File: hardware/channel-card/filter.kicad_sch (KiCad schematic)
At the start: 117 parts, among them J181 CUTOFF CV 1 V/oct, SW181 FILTER BYPASS (latching), U101 SSI2144, U102 SSI2144, U103 LM13700, U104 NE5532, U105 NE5532, U106 NE5532, U107 TL072, U108 DG413DY

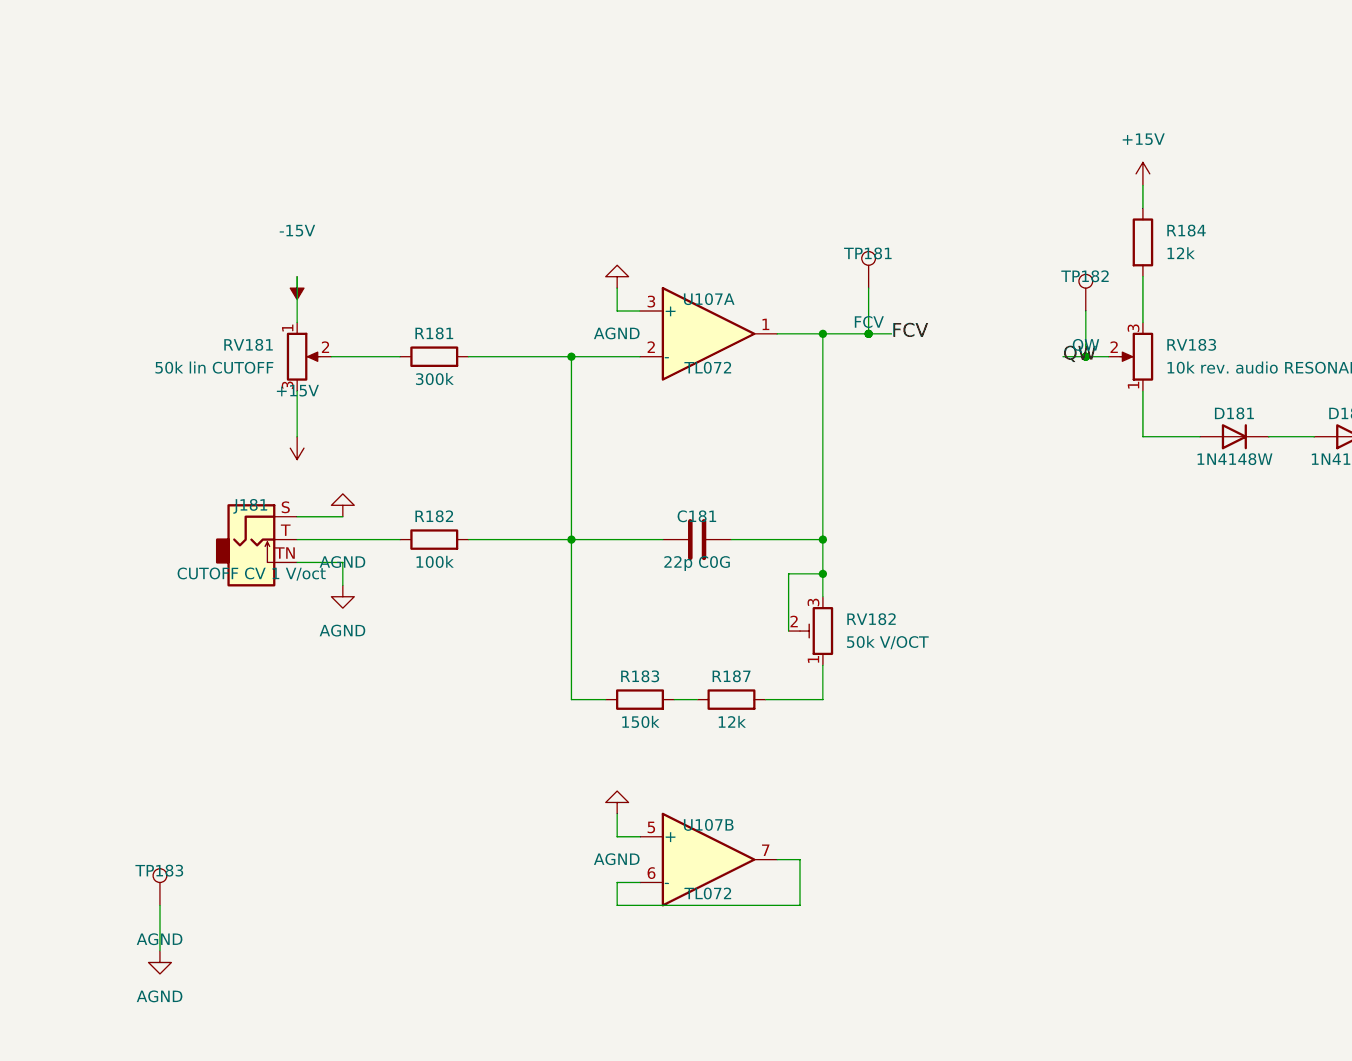
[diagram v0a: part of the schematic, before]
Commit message: Channel: cutoff CV chaining, CV OUT and summer clamp (decision 165)
CV OUT jack J182 reports the channel's total cutoff control at 1 V/oct
from FCV through the spare U107B. Jumper JP181 selects CV ONLY (a
plugged CV replaces the knob through J181's normal contact) or CV + POT.
D184/D185 BZT52C11 back to back clamp the cutoff summer so the SSI2144
frequency pin stays within about +-128 mV (datasheet range -120..+150 mV,
dropout above about +175 mV); simulation/cutoff/, breadboard test 13.
Panel row for CV IN/OUT noted for /system.

Co-Authored-By: Claude Opus 5.5 <noreply@anthropic.com>
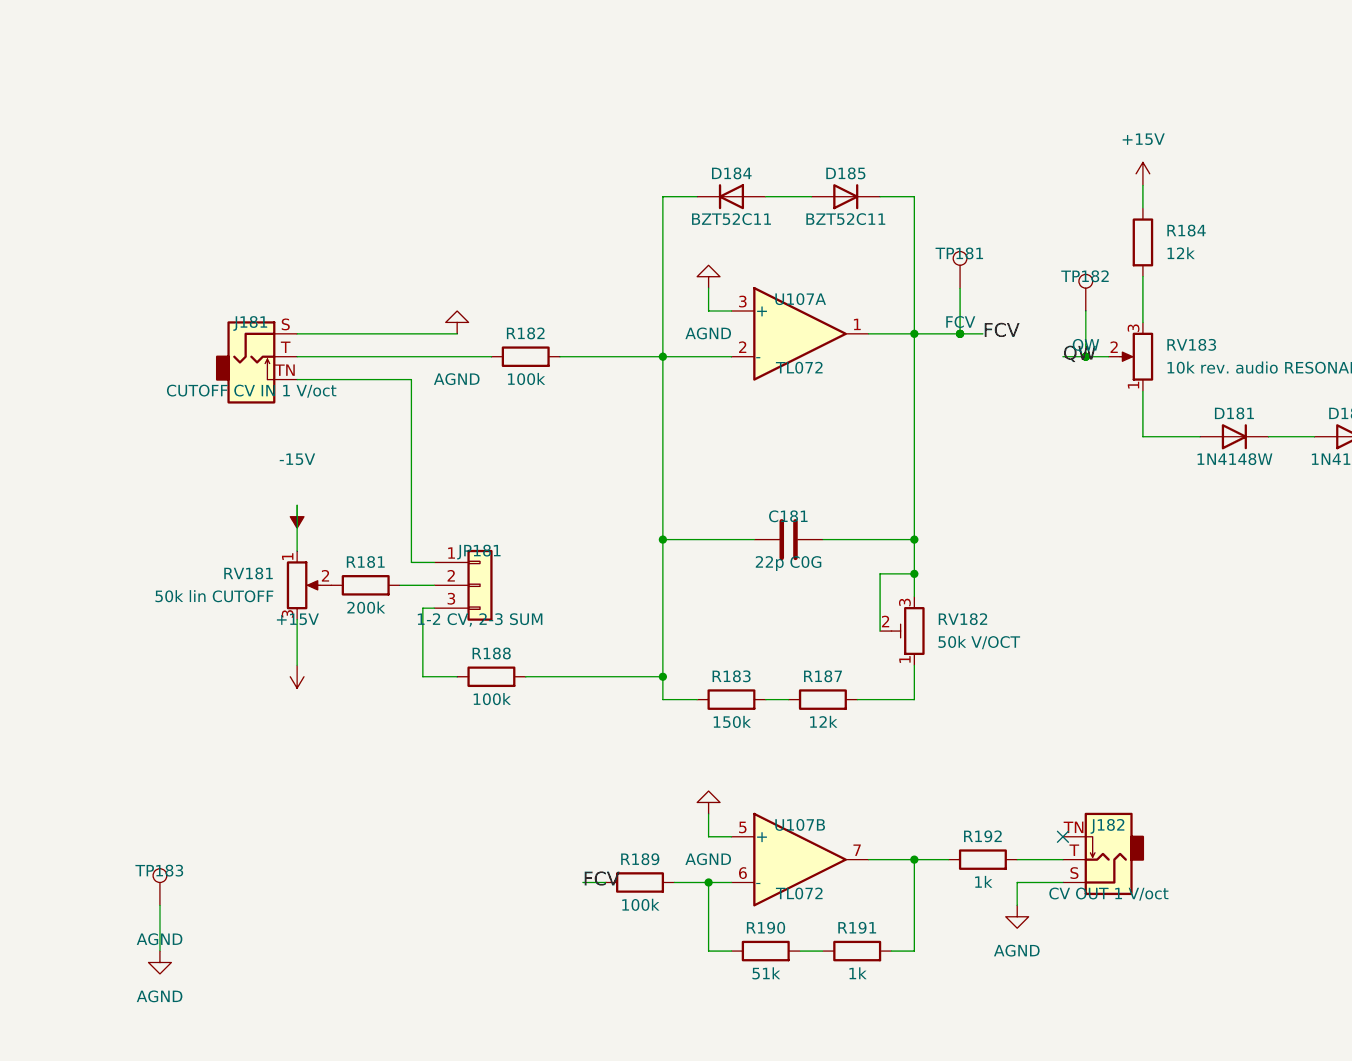
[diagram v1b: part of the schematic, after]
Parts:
- added D184, D185: BZT52C11, Diode_SMD:D_SOD-123, symbol Device:D
- added J182: CV OUT 1 V/oct, Connector_Audio:Jack_3.5mm_QingPu_WQP-PJ398SM_Vertical_CircularHoles, symbol Connector_Audio:AudioJack2_SwitchT
- added JP181: 1-2 CV, 2-3 SUM, Connector_PinHeader_2.54mm:PinHeader_1x03_P2.54mm_Vertical, symbol Connector_Generic:Conn_01x03
- added R188, R189: 100k, Resistor_SMD:R_0805_2012Metric, symbol Device:R
- added R190: 51k, Resistor_SMD:R_0805_2012Metric, symbol Device:R
- added R191, R192: 1k, Resistor_SMD:R_0805_2012Metric, symbol Device:R
- J181: value CUTOFF CV 1 V/oct -> CUTOFF CV IN 1 V/oct; Note 3.5 mm Thonkiconn on the top panel with a 1 mm M6 washer (SX-MECH-004); 3 mm PCB hole under the barrel -> 3.5 mm Thonkiconn on the top panel with a 1 mm M6 washer (SX-MECH-004); 3 mm PCB hole under the barrel; normal contact TN to JP181 (decision 165)
- R181: value 300k -> 200k; Note (none) -> With R188 100k the pot leg is 300k in either jumper positio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; ProjectPN SX-R-096 -> SX-R-116
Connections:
- net AGND: now also J182.S; no longer J181.TN
- net FCV: now also D185.1 (K), R189.1
- net at C181.1, R182.2, R183.1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: now also D184.1 (K), R188.2; no longer R181.2
- net at U107.7: now also R191.2, R192.1; no longer U107.6 (-)
- new net: J182.T, R192.2
- new net: JP181.2 (Pin_2), R181.2
- new net: D184.2 (A), D185.2 (A)
- new net: JP181.3 (Pin_3), R188.1
- new net: R190.2, R191.1
- new net: J181.TN, JP181.1 (Pin_1)
- new net: R189.2, R190.1, U107.6 (-)
- no-connect marks 6 -> 7

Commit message: Channel card: CD4052B bus assign, PFL and SC send switches at the virtual-earth bus ends, LCSC BOCHEN trimmers (decisions 183-184)
Co-Authored-By: Claude Opus 5.5 <noreply@anthropic.com>
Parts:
- RV101, RV151, RV182: MPN 3296W-1-503LF -> 3296W-1-503; Manufacturer Bourns -> BOCHEN; ProjectPN SX-TRIM-001 -> SX-TRIM-002; Supplier Mouser -> LCSC; SupplierPN 652-3296W-1-503LF -> C118911
